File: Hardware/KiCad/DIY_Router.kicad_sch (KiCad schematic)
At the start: 28 parts, among them IC1 HLK-7628N, IC2 TPS62A06ADRLR, J1 217179-0001, J5 Conn_01x06_Pin, J6 Conn_02x07_Odd_Even, SW1 SW_Push, SW2 SW_Push, U2 USBLC6-2SC6Y

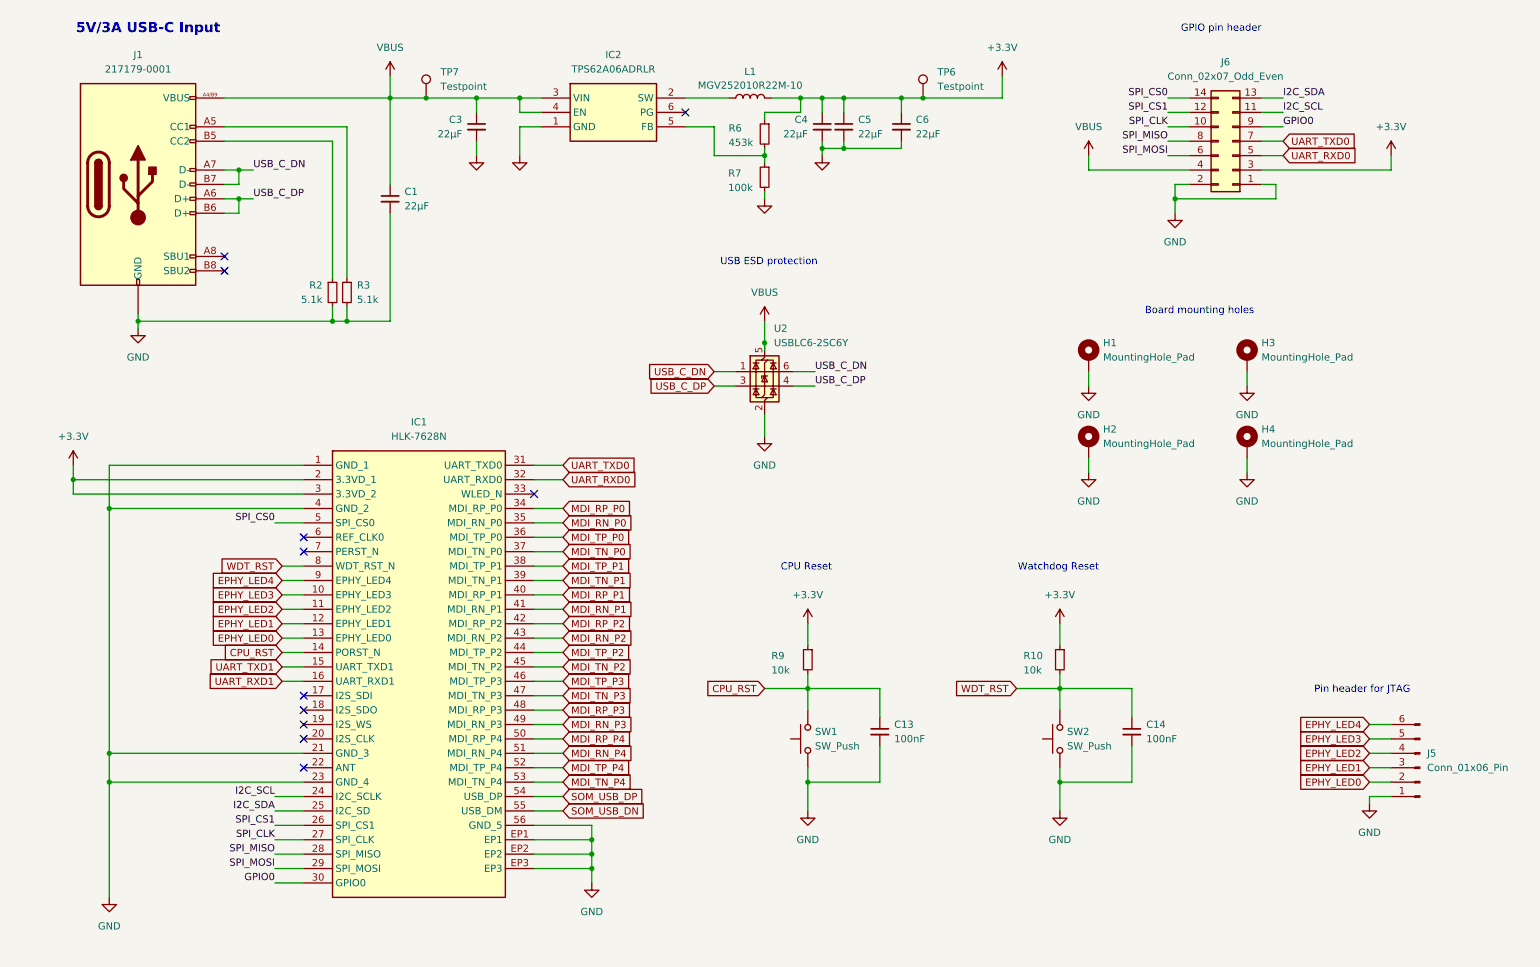
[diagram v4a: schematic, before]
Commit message: Add switches for cpu reset and watchdog reset Add swtich for WWAN wirless disable Fix USB2422 VBUS-DET and NON_REM strap pins
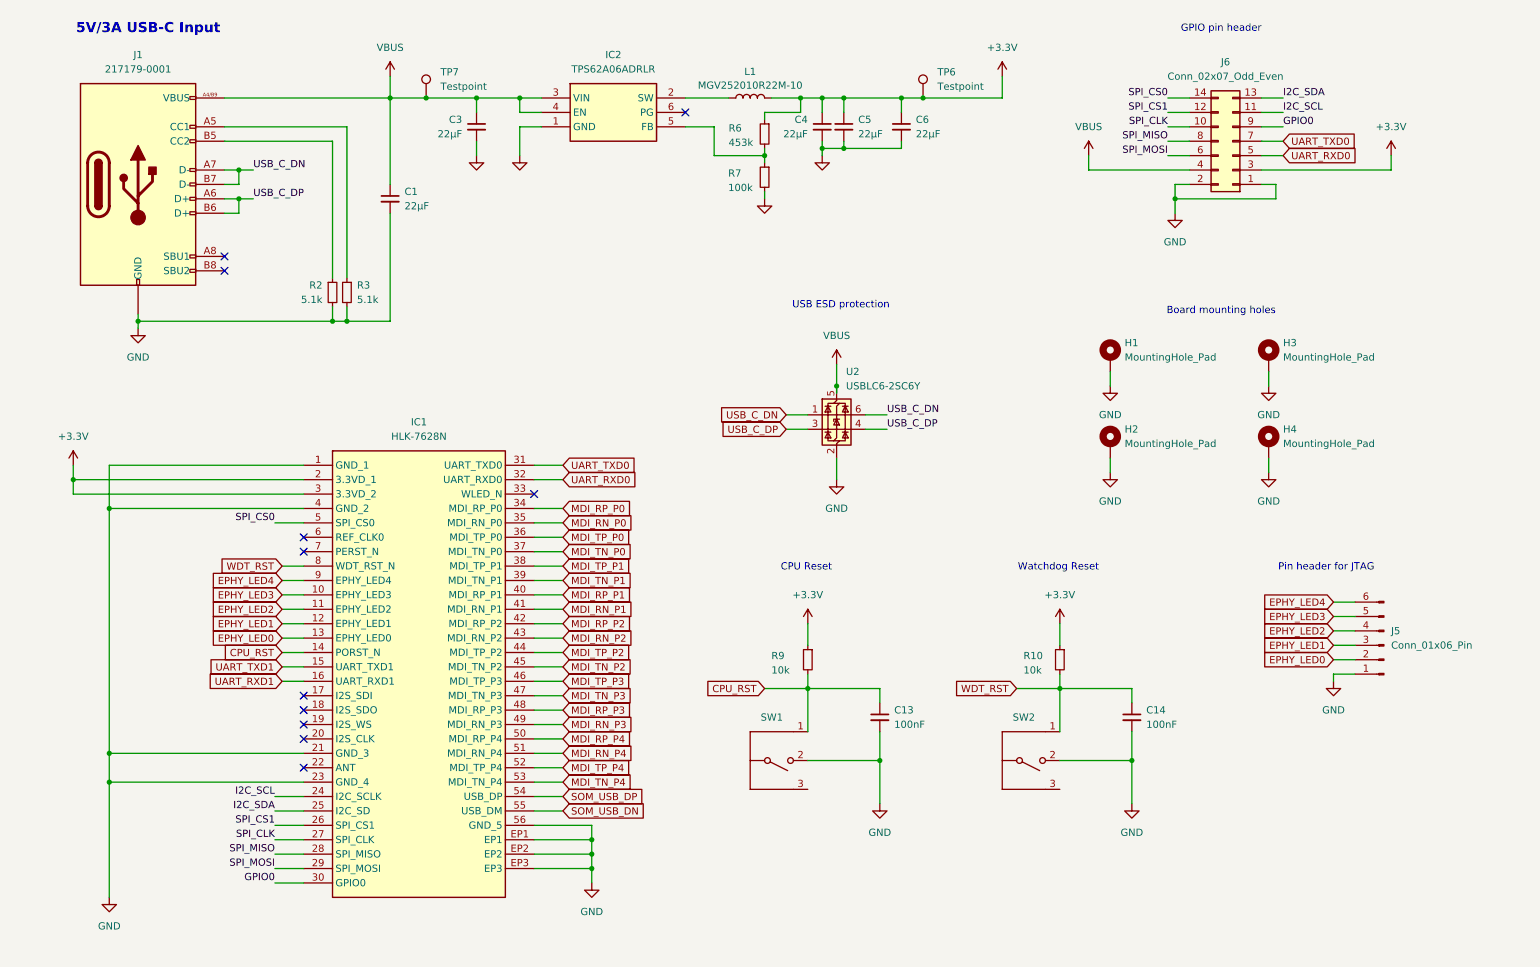
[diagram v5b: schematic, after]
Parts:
- removed SW1, SW2: SW_Push, Button_Switch_SMD:SW_Push_1P1T-MP_NO_Horizontal_Alps_SKRTLAE010, symbol Switch:SW_Push
- added SW1, SW2: 436333033816, WS-TASU:SW_Wurth_WS-TASU_436333033816, symbol WS-TASU:436333033816
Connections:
- net CPU_RST: now also SW1.1 (A)
- net GND: now also SW1.2, SW2.2
- net WDT_RST: now also SW2.1 (A)
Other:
- moved on the sheet: C13, C14, H1, H2, H3, H4, J5, U2

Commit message: Fix footprints for Mini PCIe and switches (set pads for mounting and case to GND) Set PCB to 4 layer with 0.5 OZ (0,017mm) copper on the inner layers Start sorting the footprints on the PCB TO-DO: check footprints of Y1 and Y2, they seem way too large
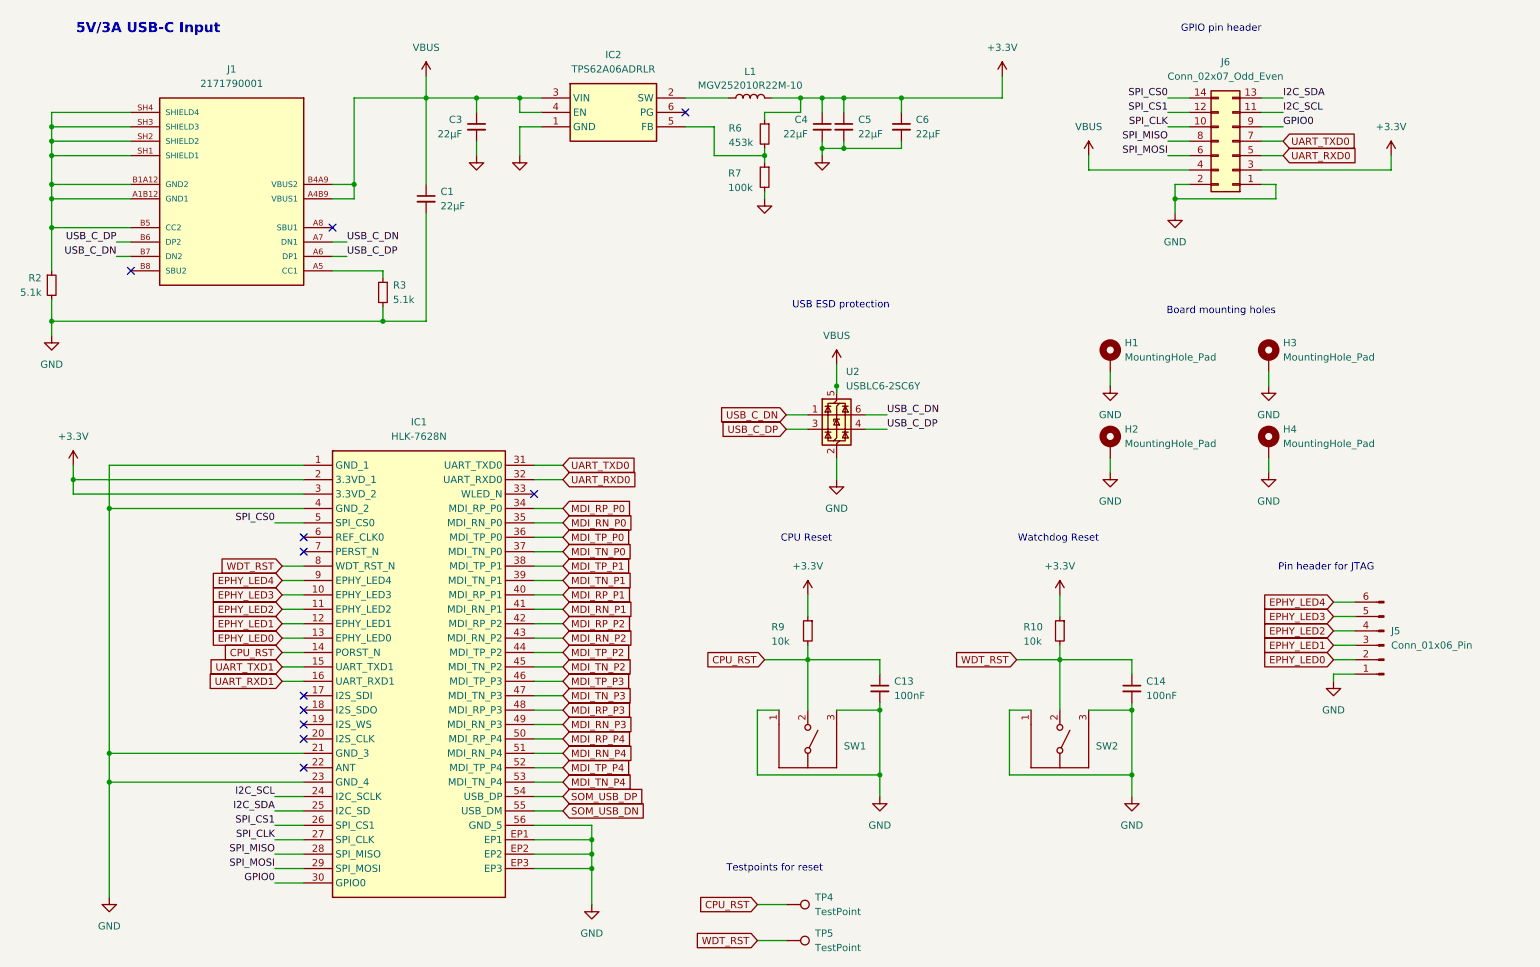
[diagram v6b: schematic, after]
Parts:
- removed J1: 217179-0001, 2171790001:MOLEX_2171790001, symbol Connector:USB_C_Receptacle_USB2.0_16P
- removed TP6, TP7: Testpoint, symbol Connector:TestPoint
- added J1: 2171790001, 2171790001:MOLEX_2171790001, symbol 2171790001:2171790001
- added TP4, TP5: TestPoint, TestPoint:TestPoint_Pad_D2.0mm, symbol Connector:TestPoint
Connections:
- net CPU_RST: now also SW1.2, TP4.1; no longer SW1.1 (A)
- net GND: now also SW1.1 (A), SW1.3, SW2.1 (A), SW2.3; no longer SW1.2, SW2.2
- net USB_C_DN: now also J1.A7 (DN1), J1.B7 (DN2)
- net USB_C_DP: now also J1.A6 (DP1), J1.B6 (DP2)
- net VBUS: now also J1.A4B9 (VBUS1), J1.B4A9 (VBUS2)
- net WDT_RST: now also SW2.2, TP5.1; no longer SW2.1 (A)
- net at R3.1: now also J1.A5 (CC1)
- net at R2.1: now also J1.A1B12 (GND1), J1.B1A12 (GND2), J1.B5 (CC2), J1.SH1 (SHIELD1), J1.SH2 (SHIELD2), J1.SH3 (SHIELD3), J1.SH4 (SHIELD4)
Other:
- note added: "Testpoints for reset"
- moved on the sheet: C1, C13, C14, R10, R2, R3, R9, SW1, SW2
